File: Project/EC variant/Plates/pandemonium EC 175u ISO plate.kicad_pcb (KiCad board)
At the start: 2 copper layers, 199.9 x 81 mm, 37 parts

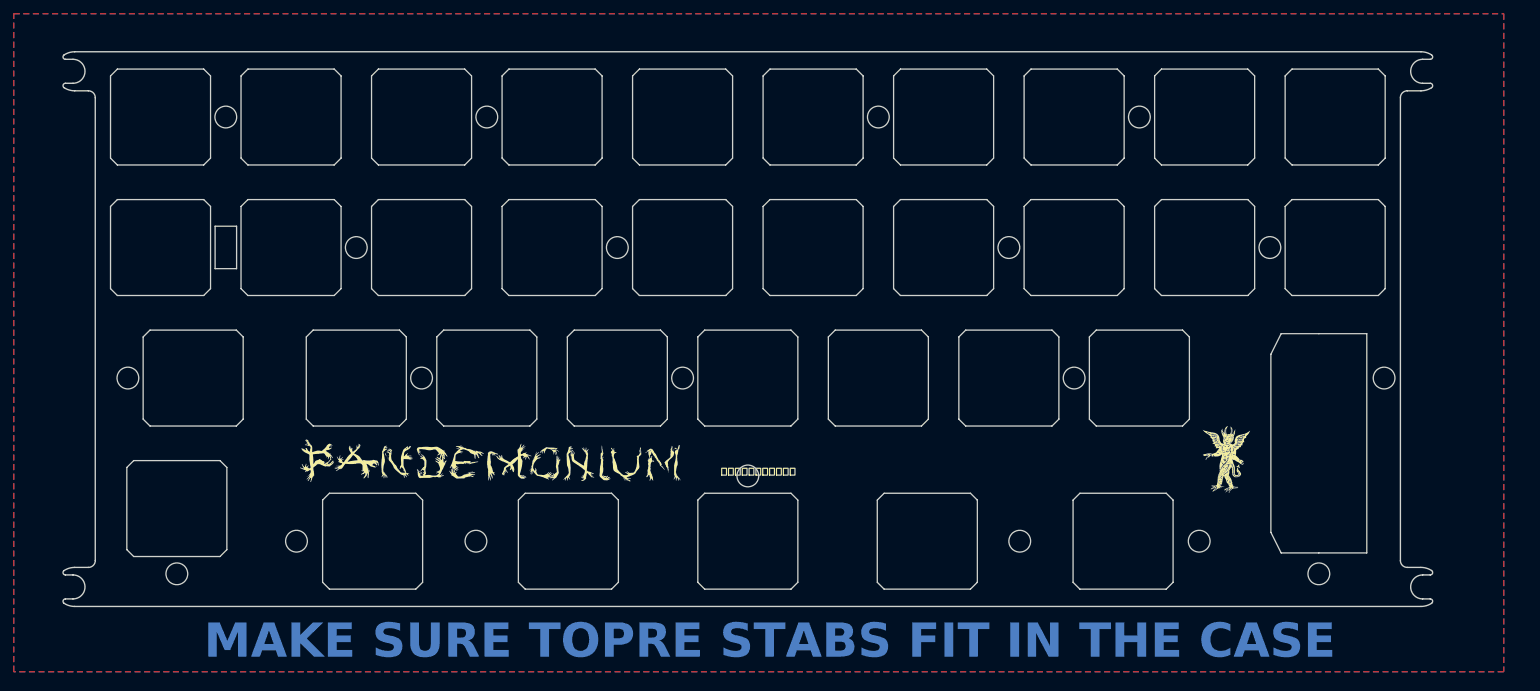
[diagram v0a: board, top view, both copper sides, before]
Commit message: changes to topre version and BLE version
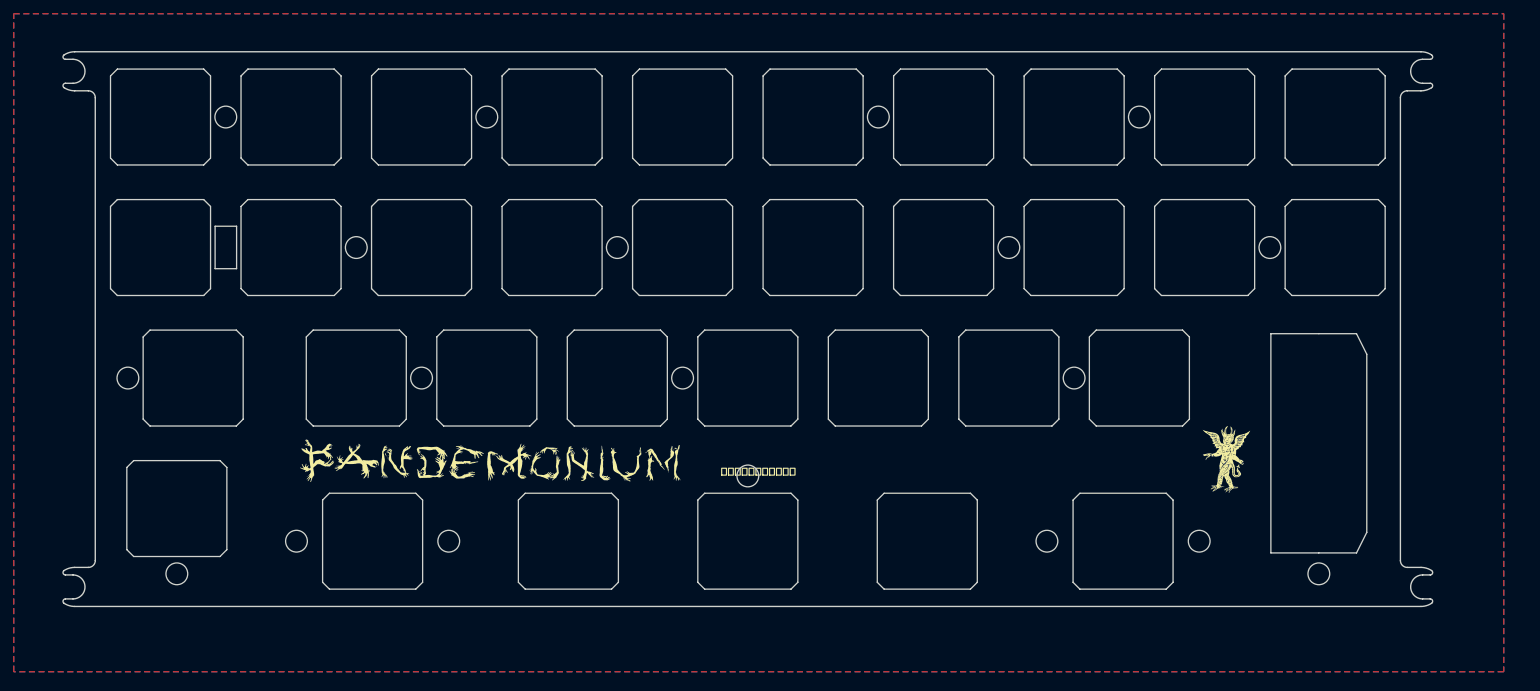
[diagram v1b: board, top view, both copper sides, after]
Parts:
- turned REF** to 90 degrees
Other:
- outline, holes or cut-outs redrawn
- board text removed: "MAKE SURE TOPRE STABS FIT IN THE CASE"
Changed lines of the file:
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@@
   )
   (footprint "cipulot_parts:ecs_plate_cut_2U" (layer "F.Cu")
-    (at 210.34375 80.9625 -90)
+    (at 210.34375 80.9625 90)
     (descr " StepUp generated footprint")
     (attr smd)
@@
   (gr_arc (start 30.75 29.5125) (mid 31.457107 29.805393) (end 31.75 30.5125)
     (stroke (width 0.2) (type solid)) (layer "Edge.Cuts"))
-  (gr_circle (center 219.86875 71.4375) (end 219.86875 69.85)
-    (stroke (width 0.1) (type default)) (fill none) (layer "Edge.Cuts"))
   (gr_line (start 226.606466 103.675) (end 225.499444 103.675)
     (stroke (width 0.2) (type solid)) (layer "Edge.Cuts"))
@@
   (gr_arc (start 226.796369 24.2685) (mid 226.942172 24.661495) (end 226.606464 24.9125)
     (stroke (width 0.2) (type solid)) (layer "Edge.Cuts"))
-  (gr_circle (center 87.3125 95.25) (end 87.3125 93.6625)
+  (gr_circle (center 83.34375 95.25) (end 83.34375 93.6625)
     (stroke (width 0.1) (type default)) (fill none) (layer "Edge.Cuts"))
   (gr_arc (start 222.25 30.5125) (mid 222.542893 29.805393) (end 223.25 29.5125)
@@
   (gr_arc (start 223.25 99.075) (mid 222.542893 98.782107) (end 222.25 98.075)
     (stroke (width 0.2) (type solid)) (layer "Edge.Cuts"))
-  (gr_circle (center 166.6875 95.25) (end 166.6875 93.6625)
+  (gr_circle (center 170.65625 95.25) (end 170.65625 93.6625)
     (stroke (width 0.1) (type default)) (fill none) (layer "Edge.Cuts"))
   (gr_arc (start 225.25 99.075) (mid 226.056102 99.191376) (end 226.796371 99.531)
@@
   (gr_arc (start 28.500556 24.9125) (mid 30.250556 26.6625) (end 28.500556 28.4125)
     (stroke (width 0.2) (type solid)) (layer "Edge.Cuts"))
-  (gr_text "MAKE SURE TOPRE STABS FIT IN THE CASE" (at 47.625 112.7125) (layer "B.Cu")
-    (effects (font (size 5 5) (thickness 0.3) bold) (justify left bottom))
-  )
   (gr_text "JLCJLCJLCJLC" (at 127 25.4) (layer "B.SilkS")
     (effects (font (size 1 1) (thickness 0.15)))
